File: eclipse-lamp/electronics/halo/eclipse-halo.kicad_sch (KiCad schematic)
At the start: 46 parts, among them J1 TO CORE

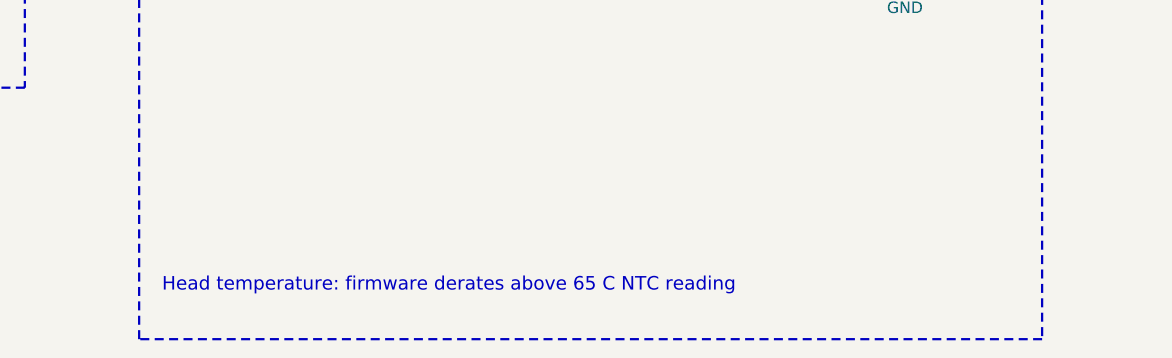
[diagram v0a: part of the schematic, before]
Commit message: ECLIPSE: light emanates through the body (diffusion redesign)
- Halo is now a hollow light-diffusing PMMA body under a thin graphite cap;
  the LED board fires down into it, so the underside gives task light and
  the walls glow with a soft falloff toward the cap
- Base gains a glowing opal band lit by an internal light chamber (white
  steel reflector/weight); steel plinth keeps the CoG 40 mm inside the edge
- Core board: 8 rim 2835 LEDs + AO3400A on PC0 (TCD0 PWM) for the base glow;
  schematic fully wired (no labels), ERC/DRC clean, re-routed, fab re-exported
- Renders: glow-material shader, new close-up and night-glow shots
- BOM, README and design notes updated (thermal/PMMA margin, stability)

Co-Authored-By: Claude Opus 5.5 <noreply@anthropic.com>
Claude-Session: https://claude.ai/code/session_01UC4Dpjx8nsVkJqTcucsgsg
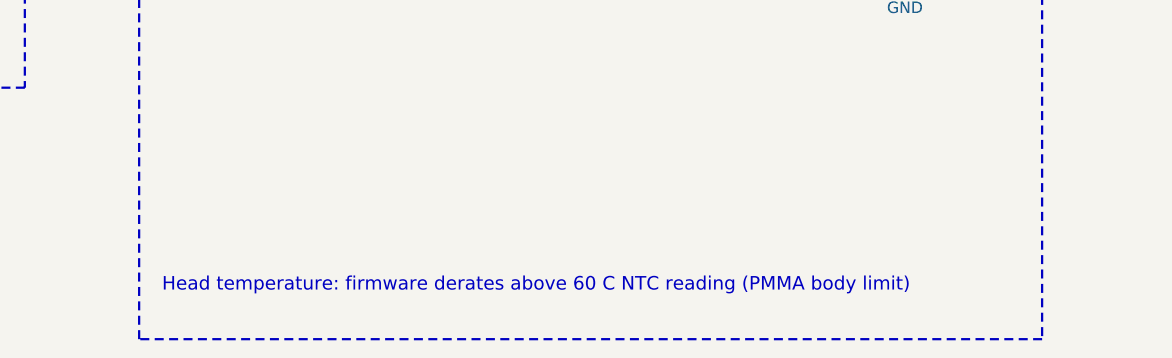
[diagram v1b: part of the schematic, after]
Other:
- note added: "Head temperature: firmware derates above 60 C NTC reading (PMMA body limit)"
- note removed: "Head temperature: firmware derates above 65 C NTC reading"
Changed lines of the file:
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@@
 		)
 	)
-	(text "Head temperature: firmware derates above 65 C NTC reading"
+	(text "Head temperature: firmware derates above 60 C NTC reading (PMMA body limit)"
 		(exclude_from_sim no)
 		(at 302.26 185.42 0)
